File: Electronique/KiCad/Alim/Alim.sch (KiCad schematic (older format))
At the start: 17 parts, among them P1 CONN_2, P2 CONN_2, P3 CONN_2, P4 CONN_2, P5 CONN_2, P6 CONN_2, P7 CONN_2, P8 CONN_2, T1 MMBT2907A, T3 NJVMJD44H11

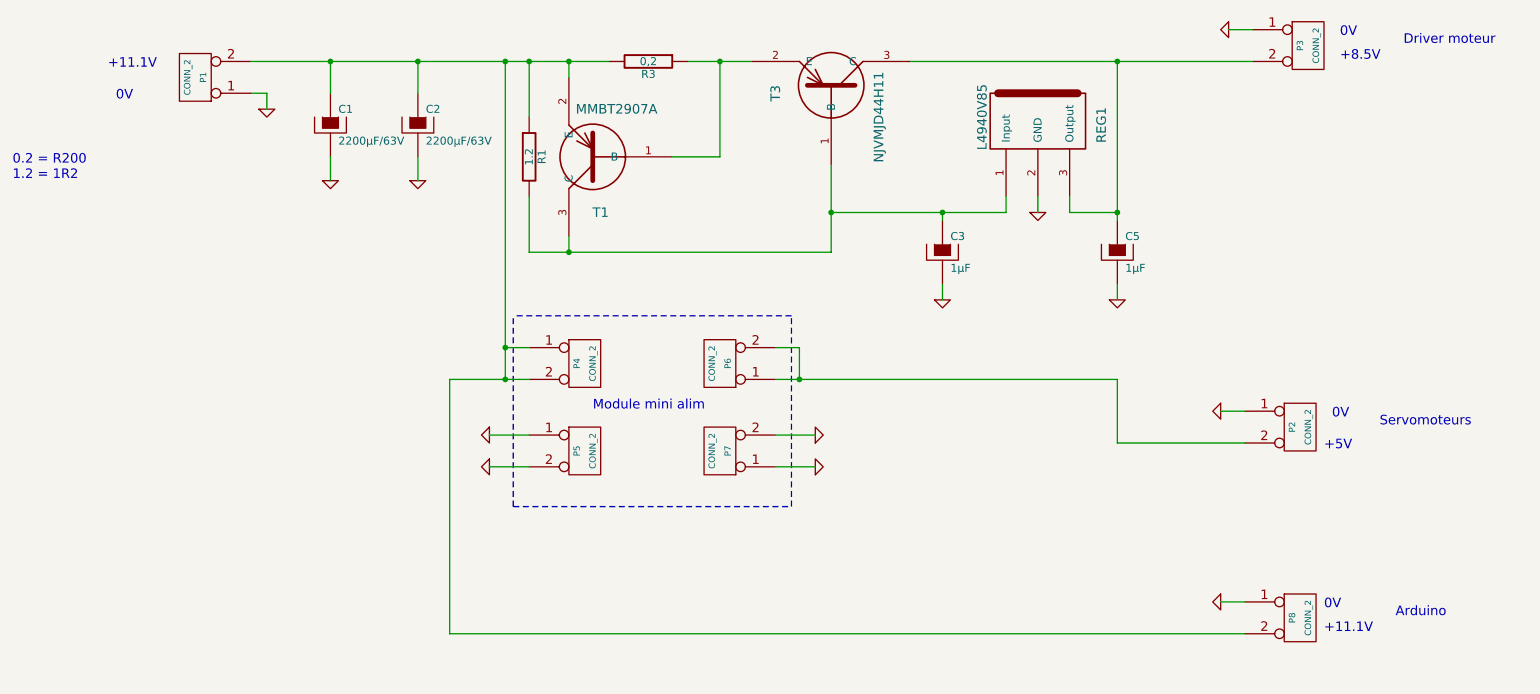
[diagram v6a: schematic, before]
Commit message: Mise à jour de la carte Rectification d'une erreur concernant le T2 qui est un MJD45H11G
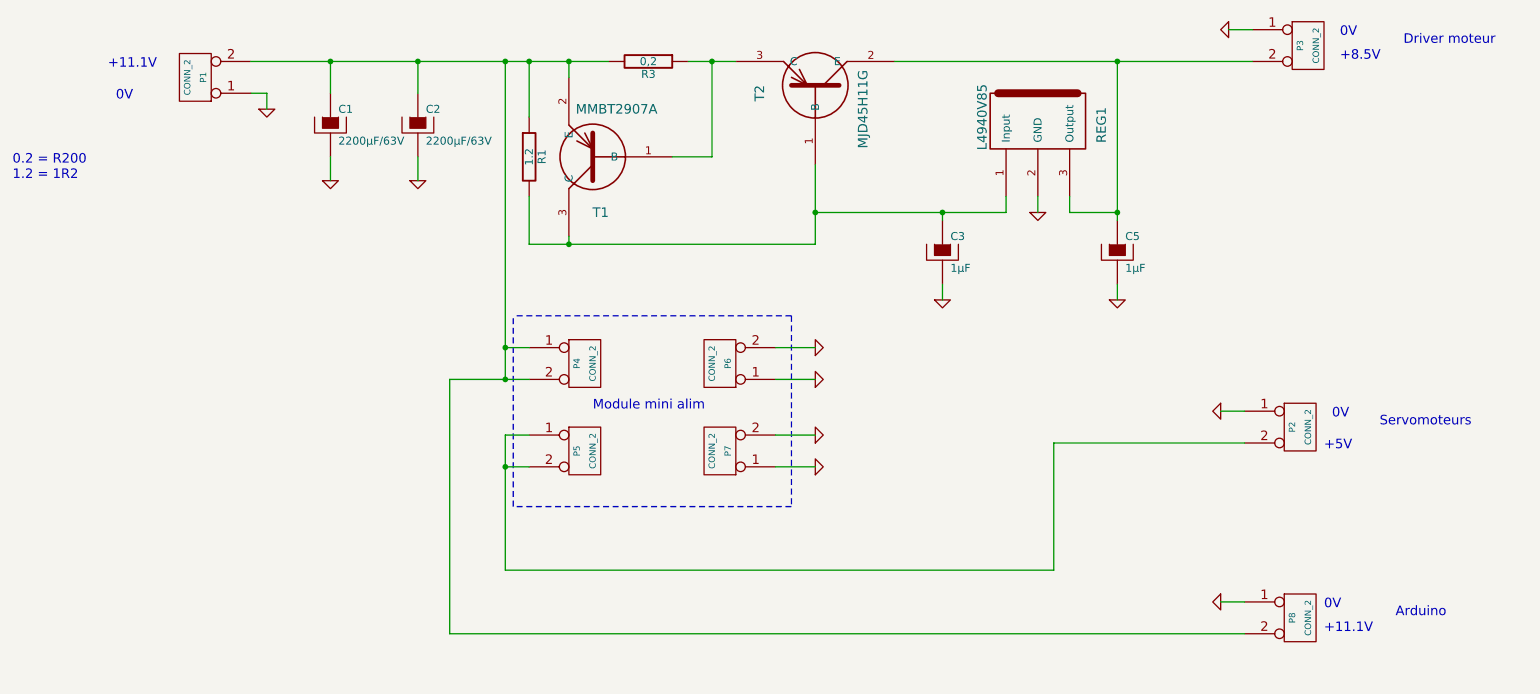
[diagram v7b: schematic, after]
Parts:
- removed T3: NJVMJD44H11, symbol NJVMJD44H11
- added T2: MJD45H11G, symbol MJD45H11G
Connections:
- net GND: now also P6.1 (P1), P6.2 (PM); no longer P5.1 (P1), P5.2 (PM)
- net at R3.1, T1.1 (B): now also T2.3 (C)
- net at C3.1, R1.2, REG1.1 (Input)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: now also T2.1 (B)
- net at C5.1, P3.2 (PM), REG1.3 (Output): now also T2.2 (E)
- new net: P2.2 (PM), P5.1 (P1), P5.2 (PM)
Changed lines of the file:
@@
-EESchema Schematic File Version 2  date lun. 15 déc. 2014 23:51:44 CET
+EESchema Schematic File Version 2  date mar. 06 janv. 2015 19:47:28 CET
 LIBS:power
 LIBS:device
@@
 Sheet 1 1
 Title ""
-Date "15 dec 2014"
+Date "6 jan 2015"
 Rev ""
 Comp ""
@@
 Comment4 ""
 $EndDescr
-Connection ~ 4050 3700
-Wire Wire Line
-	8700 5300 3700 5300
-Wire Wire Line
-	3700 5300 3700 3700
-Wire Wire Line
-	3700 3700 4200 3700
-Wire Wire Line
-	5750 4250 6000 4250
-Wire Wire Line
-	3950 4250 4200 4250
-Connection ~ 5900 3700
-Wire Wire Line
-	8700 4100 7900 4100
-Wire Wire Line
-	7900 4100 7900 3700
-Wire Wire Line
-	7900 3700 5750 3700
-Connection ~ 4050 3500
-Wire Wire Line
-	4050 3700 4050 1700
+Wire Wire Line
+	5750 3700 6000 3700
+Connection ~ 4050 4250
+Wire Wire Line
+	8700 4100 7500 4100
+Wire Wire Line
+	7500 4100 7500 4900
+Wire Wire Line
+	7500 4900 4050 4900
+Wire Wire Line
+	4050 4900 4050 4050
+Connection ~ 7900 1700
+Wire Wire Line
+	6500 1700 8750 1700
+Wire Wire Line
+	7900 2650 7600 2650
+Wire Wire Line
+	7600 2650 7600 2550
+Connection ~ 6000 2650
+Wire Wire Line
+	6800 2650 6800 2700
+Wire Wire Line
+	4450 2850 4450 2800
+Wire Wire Line
+	4200 2550 4200 2850
+Wire Wire Line
+	5200 1700 5500 1700
+Wire Wire Line
+	8700 5100 8550 5100
+Wire Wire Line
+	5750 4050 6000 4050
+Connection ~ 4050 1700
+Wire Wire Line
+	4050 3500 4200 3500
+Wire Wire Line
+	3500 2300 3500 2450
+Connection ~ 3500 1700
+Wire Wire Line
+	3500 1700 3500 1900
+Wire Wire Line
+	2550 2000 2550 1900
+Wire Wire Line
+	2550 1900 2450 1900
+Wire Wire Line
+	6800 3200 6800 3100
+Connection ~ 4200 1700
+Wire Wire Line
+	4200 1700 4200 2050
+Connection ~ 4450 1700
+Wire Wire Line
+	4450 1800 4450 1700
+Wire Wire Line
+	7400 2650 7400 2550
+Wire Wire Line
+	7900 3200 7900 3100
+Wire Wire Line
+	8750 1500 8600 1500
+Wire Wire Line
+	8700 3900 8550 3900
+Wire Wire Line
+	4700 1700 2450 1700
+Wire Wire Line
+	2950 1900 2950 1700
+Connection ~ 2950 1700
+Wire Wire Line
+	2950 2300 2950 2450
+Wire Notes Line
+	5850 3300 4100 3300
+Wire Notes Line
+	5850 3300 5850 4500
+Wire Notes Line
+	5850 4500 4100 4500
 Wire Notes Line
 	4100 4500 4100 3300
-Wire Notes Line
-	4100 4500 5850 4500
-Wire Notes Line
-	5850 4500 5850 3300
-Wire Notes Line
-	5850 3300 4100 3300
-Wire Wire Line
-	2950 2300 2950 2450
-Connection ~ 2950 1700
-Wire Wire Line
-	2950 1900 2950 1700
-Wire Wire Line
-	4700 1700 2450 1700
-Wire Wire Line
-	8700 3900 8550 3900
-Wire Wire Line
-	8750 1500 8600 1500
-Wire Wire Line
-	7900 3200 7900 3100
+Wire Wire Line
+	4050 3700 4050 1700
+Connection ~ 4050 3500
+Wire Wire Line
+	5750 4250 6000 4250
+Wire Wire Line
+	4200 3700 3700 3700
+Wire Wire Line
+	3700 3700 3700 5300
+Wire Wire Line
+	3700 5300 8700 5300
+Connection ~ 4050 3700
+Wire Wire Line
+	5100 2300 5350 2300
+Wire Wire Line
+	5350 2300 5350 1700
+Connection ~ 5350 1700
+Wire Wire Line
+	4200 2850 6000 2850
+Wire Wire Line
+	6000 2850 6000 2350
+Connection ~ 4450 2850
+Wire Wire Line
+	6000 2650 7200 2650
+Wire Wire Line
+	7200 2650 7200 2550
 Connection ~ 6800 2650
-Connection ~ 6100 2650
-Wire Wire Line
-	6100 2650 7200 2650
-Wire Wire Line
-	7400 2650 7400 2550
-Wire Wire Line
-	7900 2700 7900 1700
-Wire Wire Line
-	5600 1700 5200 1700
-Wire Wire Line
-	6100 2350 6100 2900
-Wire Wire Line
-	6100 2900 4200 2900
-Wire Wire Line
-	4200 2900 4200 2550
-Wire Wire Line
-	4450 1800 4450 1700
-Connection ~ 4450 1700
-Wire Wire Line
-	4200 1700 4200 2050
-Connection ~ 4200 1700
-Wire Wire Line
-	4450 2800 4450 2900
-Connection ~ 4450 2900
-Wire Wire Line
-	5400 1700 5400 2300
-Wire Wire Line
-	5400 2300 5100 2300
-Connection ~ 5400 1700
-Connection ~ 7900 1700
-Wire Wire Line
-	7600 2550 7600 2650
-Wire Wire Line
-	7600 2650 7900 2650
+Wire Wire Line
+	7900 1700 7900 2700
 Connection ~ 7900 2650
 Wire Wire Line
-	7200 2650 7200 2550
-Wire Wire Line
-	6800 2700 6800 2650
-Wire Wire Line
-	6800 3200 6800 3100
-Wire Wire Line
-	6600 1700 8750 1700
-Wire Wire Line
-	2450 1900 2550 1900
-Wire Wire Line
-	2550 1900 2550 2000
-Wire Wire Line
-	3500 1700 3500 1900
-Connection ~ 3500 1700
-Wire Wire Line
-	3500 2300 3500 2450
-Wire Wire Line
-	4050 3500 4200 3500
-Connection ~ 4050 1700
-Wire Wire Line
-	5750 3500 5900 3500
-Wire Wire Line
-	5900 3500 5900 3700
-Wire Wire Line
-	3950 4050 4200 4050
-Wire Wire Line
-	5750 4050 6000 4050
-Wire Wire Line
-	8700 5100 8550 5100
+	4050 4050 4200 4050
+Wire Wire Line
+	4050 4250 4200 4250
+Wire Wire Line
+	5750 3500 6000 3500
+$Comp
+L MJD45H11G T2
+U 1 1 54AC2BB2
+P 6000 1850
+F 0 "T2" H 6050 1500 60  0000 C CNN
+F 1 "MJD45H11G" H 6150 2150 60  0000 C CNN
+	1    6000 1850
+	0    1    1    0
+$EndComp
 Text Notes 9700 1600 0    60   ~ 0
 Driver moteur
@@
 L GND #PWR04
 U 1 1 548DFE92
-P 3950 4250
-F 0 "#PWR04" H 3950 4250 30  0001 C CNN
-F 1 "GND" H 3950 4180 30  0001 C CNN
-	1    3950 4250
-	0    1    1    0
+P 6000 3700
+F 0 "#PWR04" H 6000 3700 30  0001 C CNN
+F 1 "GND" H 6000 3630 30  0001 C CNN
+	1    6000 3700
+	0    -1   -1   0
 $EndComp
 $Comp
 L GND #PWR05
 U 1 1 548DFE8A
-P 3950 4050
-F 0 "#PWR05" H 3950 4050 30  0001 C CNN
-F 1 "GND" H 3950 3980 30  0001 C CNN
-	1    3950 4050
-	0    1    1    0
+P 6000 3500
+F 0 "#PWR05" H 6000 3500 30  0001 C CNN
+F 1 "GND" H 6000 3430 30  0001 C CNN
+	1    6000 3500
+	0    -1   -1   0
 $EndComp
 Text Notes 4600 3900 0    60   ~ 0
@@
 $EndComp
 $Comp
-L NJVMJD44H11 T3
-U 1 1 54214931
-P 6100 1850
-F 0 "T3" H 6150 1500 60  0000 C CNN
-F 1 "NJVMJD44H11" H 6300 2150 60  0000 C CNN
-	1    6100 1850
-	0    1    1    0
-$EndComp
-$Comp
